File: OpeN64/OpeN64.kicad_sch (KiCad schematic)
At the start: 269 parts, among them P6 P5, SW1 N64_SW1_Power, SW2 RESET, U13 78M05, x1 Crystal_Small, x2 Crystal_Small

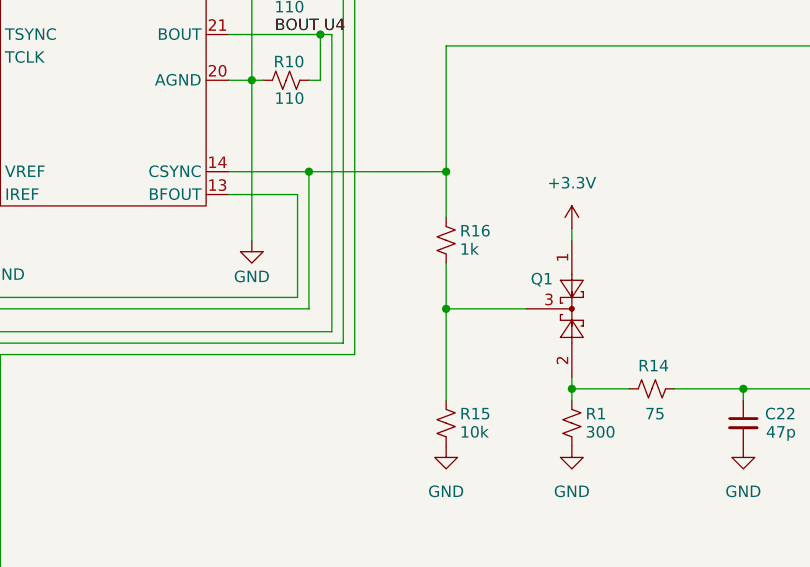
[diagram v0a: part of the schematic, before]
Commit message: correct non-schematic parity DRC errors
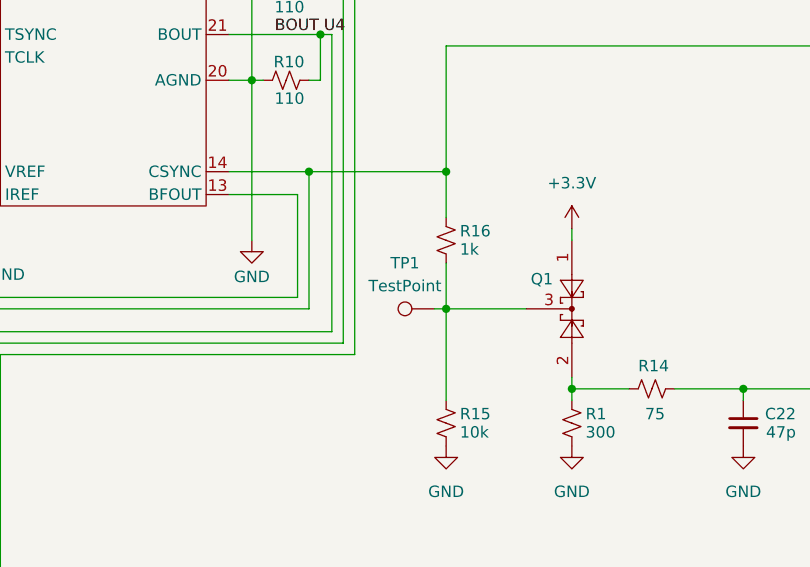
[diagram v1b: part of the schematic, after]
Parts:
- added TP1: TestPoint, TestPoint:TestPoint_Pad_D1.0mm, symbol Connector:TestPoint
- SW2: symbol Switch:SW_MEC_5G -> OpeN64:N64_SW2_Reset
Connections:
- net at Q1.3, R15.1, R16.2: now also TP1.1
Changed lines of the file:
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@@
 	(wire
 		(pts
+			(xy 833.12 492.76) (xy 834.39 492.76)
+		)
+		(stroke
+			(width 0)
+			(type default)
+		)
+	)
+	(wire
+		(pts
 			(xy 990.6 200.66) (xy 1002.03 200.66)
 		)
@@
 	)
 	(symbol
+		(lib_id "Connector:TestPoint")
+		(at 833.12 492.76 90)
+		(unit 1)
+		(exclude_from_sim no)
+		(in_bom yes)
+		(on_board yes)
+		(dnp no)
+		(fields_autoplaced yes)
+		(property "Reference" "TP1"
+			(at 829.818 487.68 90)
+			(effects
+				(font
+					(size 1.27 1.27)
+				)
+			)
+		)
+		(property "Value" "TestPoint"
+			(at 829.818 490.22 90)
+			(effects
+				(font
+					(size 1.27 1.27)
+				)
+			)
+		)
+		(property "Footprint" "TestPoint:TestPoint_Pad_D1.0mm"
+			(at 833.12 487.68 0)
+			(effects
+				(font
+					(size 1.27 1.27)
+				)
+				(hide yes)
+			)
+		)
+		(property "Datasheet" "~"
+			(at 833.12 487.68 0)
+			(effects
+				(font
+					(size 1.27 1.27)
+				)
+				(hide yes)
+			)
+		)
+		(property "Description" "test point"
+			(at 833.12 492.76 0)
+			(effects
+				(font
+					(size 1.27 1.27)
+				)
+				(hide yes)
+			)
+		)
+		(pin "1"
+		)
+		(instances
+			(project "OpeN64"
+				(path "/9cd74490-a078-4719-a3a0-1a0f47b5b270"
+					(reference "TP1")
+					(unit 1)
+				)
+			)
+		)
+	)
+	(symbol
 		(lib_id "Device:C_Small_US")
 		(at 501.65 337.82 0)
@@
 	)
 	(symbol
-		(lib_id "Switch:SW_MEC_5G")
+		(lib_id "OpeN64:N64_SW2_Reset")
 		(at 792.48 240.03 0)
 		(unit 1)
@@
 		(pin "3"
 		)
+		(pin "0"
+		)
 		(instances
